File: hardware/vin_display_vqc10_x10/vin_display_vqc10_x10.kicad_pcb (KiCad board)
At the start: 4 copper layers, 148 x 52 mm, 109 parts, among them J1 DEBUG, J2 USB_B_Micro, J3 DEBUG_UART, J4 IF_UART, J5 AUX_CONNECTOR, J6 Conn_01x02, Q1 BSS138, Q2 DMP2022LSS, Q3 DMP2022LSS, Q4 DMP2022LSS, Q5 DMP2022LSS, Q6 DMP2022LSS, Q7 DMG2301L, SW1 SW_RESET, SW2 BOOTSEL, SW3 KNOB, U1 W25Q16JVSNIQ, U10 HDSP-2000, U11 HDSP-2000, U12 HDSP-2000, U13 HDSP-2000, U14 HDSP-2000, U15 HDSP-2000, U16 HDSP-2000, U17 HDSP-2000, U18 HDSP-2000, U19 HDSP-2000, U2 MIC23050-SYML, U20 HDSP-2000, U21 HDSP-2000, U22 HDSP-2000, U23 HDSP-2000, U24 HDSP-2000, U3 RP2040, U5 HDSP-2000, U6 HDSP-2000, U7 HDSP-2000, U8 HDSP-2000, U9 HDSP-2000, X1 12MHz

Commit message: routing vqc10_x10
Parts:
- removed C28, C29, C30, C31, C32, C38, C39, C40, C41, C42: 0.1u, Capacitor_SMD:C_0603_1608Metric
- removed JP1: SolderJumper_3_Open, components:Solder_jumber_3pad
- removed Q7: DMG2301L, Package_TO_SOT_SMD:SOT-23
- removed R13: 100K, Resistor_SMD:R_0603_1608Metric
- removed U17, U18, U19, U20, U21, U22, U23, U24: HDSP-2000, components:HDSP_DIP12
- added Q8: DMP2022LSS, components:SO8_MOSFET_S3G1D4, F.Cu at (144.5, 87.1)
- added Q9: DMP2022LSS, components:SO8_MOSFET_S3G1D4, F.Cu at (144.5, 81.1)
- added R21: 100K, Resistor_SMD:R_0603_1608Metric, F.Cu at (96.0, 97.4)
- added U4: VQC10, components:VQC10, B.Cu at (341.6, 94.7)
- R14: value 100R -> 10K; footprint Resistor_SMD:R_0603_1608Metric -> Capacitor_SMD:C_0603_1608Metric
- R15: value 100R -> 100K
- U10, U11, U12, U13, U5, U6, U7, U8, U9: value HDSP-2000 -> VQC10; footprint components:HDSP_DIP12 -> components:VQC10
- U14, U15, U16: value HDSP-2000 -> 74HCT154; footprint components:HDSP_DIP12 -> Package_SO:TSSOP-24_4.4x7.8mm_P0.65mm; moved to F.Cu
- moved U9 170.0 mm to (341.6, 122.4)
- moved C37 133.6 mm to (309.3, 124.5), turned to 0 degrees
- moved C27 132.6 mm to (309.3, 96.9), turned to 0 degrees
- moved SW1 97.9 mm to (320.2, 114.0)
- moved R1 97.7 mm to (334.5, 114.7)
- moved SW2 97.7 mm to (329.1, 114.0)
- moved J5 96.7 mm to (113.3, 77.0)
- moved C33 96.2 mm to (147.8, 124.5)
- moved C23 94.6 mm to (147.8, 96.9)
- moved U14 89.6 mm to (263.8, 86.3), turned to -90 degrees
- moved C36 76.7 mm to (268.9, 124.6), turned to 0 degrees
- moved C26 74.9 mm to (269.0, 96.9), turned to 0 degrees
- moved R14 74.1 mm to (92.0, 99.9)
- moved R15 71.9 mm to (92.0, 102.4)
- moved U10 59.5 mm to (301.2, 122.4)
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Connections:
- J5 pad 4: GP14 -> GND
- J5 pad 6: GP15 -> GP18
- Q2 pad 2: DISP_COL1 -> DISP_R1
- Q2 pad 3: DRV_COL1 -> DRV_R1
- Q3 pad 2: DISP_COL2 -> DISP_R2
- Q3 pad 3: DRV_COL2 -> DRV_R2
- Q4 pad 2: DISP_COL3 -> DISP_R3
- Q4 pad 3: DRV_COL3 -> DRV_R3
- Q5 pad 2: DISP_COL4 -> DISP_R4
- Q5 pad 3: DRV_COL4 -> DRV_R4
- Q6 pad 2: DISP_COL5 -> DISP_R5
- Q6 pad 3: DRV_COL5 -> DRV_R5
- R14 pad 1: Net-(U24-DOUT) -> GND
- R14 pad 2: GND -> Net-(U16-Y10)
- R15 pad 1: D10_DOUT -> 3V3
- R15 pad 2: GND -> DISP_R1
- R16 pad 2: DISP_COL1 -> DISP_R2
- R17 pad 2: DISP_COL2 -> DISP_R3
- R18 pad 2: DISP_COL3 -> DISP_R4
- R19 pad 2: DISP_COL4 -> DISP_R5
- R20 pad 2: DISP_COL5 -> DISP_R6
- U10 pad 1: DRV_COL1 -> DISP_D1
- U10 pad 10: DISP_CLK -> GND
- U10 pad 11: GND -> DISP_D4
- U10 pad 12: D5_DOUT -> DISP_C28
- U10 pad 2: DRV_COL2 -> DISP_C25
- U10 pad 3: DRV_COL3 -> GND
- U10 pad 4: DRV_COL4 -> DISP_D3
- U10 pad 5: DRV_COL5 -> DISP_C26
- U10 pad 6: unconnected-(U10-NC-Pad6) -> GND
- U10 pad 7: Net-(U10-DOUT) -> unconnected-(U10-IV-Pad7)
- U10 pad 8: DISP_VB -> DISP_D2
- U10 pad 9: DISP_VCC -> DISP_C27
- U11 pad 1: DRV_COL1 -> DISP_D1
- U11 pad 10: DISP_CLK -> GND
- U11 pad 11: GND -> DISP_D4
- U11 pad 12: Net-(U10-DOUT) -> DISP_C32
- U11 pad 2: DRV_COL2 -> DISP_C29
- U11 pad 3: DRV_COL3 -> GND
- U11 pad 4: DRV_COL4 -> DISP_D3
- U11 pad 5: DRV_COL5 -> DISP_C30
- U11 pad 6: unconnected-(U11-NC-Pad6) -> GND
- U11 pad 7: Net-(U11-DOUT) -> unconnected-(U11-IV-Pad7)
- U11 pad 8: DISP_VB -> DISP_D2
- U11 pad 9: DISP_VCC -> DISP_C31
- U12 pad 1: DRV_COL1 -> DISP_D1
- U12 pad 10: DISP_CLK -> GND
- U12 pad 11: GND -> DISP_D4
- U12 pad 12: Net-(U11-DOUT) -> DISP_C36
- U12 pad 2: DRV_COL2 -> DISP_C33
- U12 pad 3: DRV_COL3 -> GND
- U12 pad 4: DRV_COL4 -> DISP_D3
- U12 pad 5: DRV_COL5 -> DISP_C34
- U12 pad 6: unconnected-(U12-NC-Pad6) -> GND
- U12 pad 7: Net-(U12-DOUT) -> unconnected-(U12-IV-Pad7)
- U12 pad 8: DISP_VB -> DISP_D2
- U12 pad 9: DISP_VCC -> DISP_C35
- U13 pad 1: DRV_COL1 -> DISP_D1
- U13 pad 10: DISP_CLK -> GND
- U13 pad 11: GND -> DISP_D4
- U13 pad 12: Net-(U12-DOUT) -> DISP_C40
- U13 pad 2: DRV_COL2 -> DISP_C37
- U13 pad 3: DRV_COL3 -> GND
- U13 pad 4: DRV_COL4 -> DISP_D3
- U13 pad 5: DRV_COL5 -> DISP_C38
- U13 pad 6: unconnected-(U13-NC-Pad6) -> GND
- U13 pad 7: Net-(U13-DOUT) -> unconnected-(U13-IV-Pad7)
- U13 pad 8: DISP_VB -> DISP_D2
- U13 pad 9: DISP_VCC -> DISP_C39
- U14 pad 1: DRV_COL1 -> DISP_C1
- U14 pad 10: DISP_CLK -> DISP_C10
- U14 pad 11: GND -> DISP_C11
- U14 pad 12: Net-(U13-DOUT) -> GND
- U14 pad 2: DRV_COL2 -> DISP_C2
- U14 pad 3: DRV_COL3 -> DISP_C3
- U14 pad 4: DRV_COL4 -> DISP_C4
- U14 pad 5: DRV_COL5 -> DISP_C5
- U14 pad 6: unconnected-(U14-NC-Pad6) -> DISP_C6
- U14 pad 7: D10_DOUT -> DISP_C7
- U14 pad 8: DISP_VB -> DISP_C8
- U14 pad 9: DISP_VCC -> DISP_C9
- U15 pad 1: DRV_COL1 -> DISP_C17
- U15 pad 10: DISP_CLK -> DISP_C26
- U15 pad 11: GND -> DISP_C27
- U15 pad 12: Net-(JP1-C) -> GND
- U15 pad 2: DRV_COL2 -> DISP_C18
- U15 pad 3: DRV_COL3 -> DISP_C19
- U15 pad 4: DRV_COL4 -> DISP_C20
- U15 pad 5: DRV_COL5 -> DISP_C21
- U15 pad 6: unconnected-(U15-NC-Pad6) -> DISP_C22
- U15 pad 7: Net-(U15-DOUT) -> DISP_C23
- U15 pad 8: DISP_VB -> DISP_C24
- U15 pad 9: DISP_VCC -> DISP_C25
- U16 pad 1: DRV_COL1 -> DISP_C33
- U16 pad 10: DISP_CLK -> Net-(U16-Y10)
- U16 pad 11: GND -> Net-(U16-Y10)
- U16 pad 12: Net-(U15-DOUT) -> GND
- U16 pad 2: DRV_COL2 -> DISP_C34
- U16 pad 3: DRV_COL3 -> DISP_C35
- U16 pad 4: DRV_COL4 -> DISP_C36
- U16 pad 5: DRV_COL5 -> DISP_C37
- U16 pad 6: unconnected-(U16-NC-Pad6) -> DISP_C38
- U16 pad 7: Net-(U16-DOUT) -> DISP_C39
- U16 pad 8: DISP_VB -> DISP_C40
- U16 pad 9: DISP_VCC -> Net-(U16-Y10)
- U3 pad 11: DISP_COL2 -> DISP_R3
- U3 pad 12: DISP_COL3 -> DISP_R4
- U3 pad 13: DISP_COL4 -> DISP_R5
- U3 pad 14: DISP_COL5 -> DISP_R6
- U3 pad 15: DISP_BR -> DISP_R7
- U3 pad 16: GP13 -> DISP_C_E3
- U3 pad 17: GP14 -> DISP_C_A0
- U3 pad 18: GP15 -> DISP_C_A1
- U3 pad 27: GP16 -> DISP_C_A2
- U3 pad 28: GP17 -> DISP_C_A3
- U3 pad 30: GP19 -> DISP_D1
- U3 pad 31: GP20 -> DISP_D2
- U3 pad 32: GP21 -> DISP_D3
- U3 pad 34: GP22 -> DISP_D4
- U3 pad 35: GP23 -> DISP_D5
- U3 pad 4: DISP_DATA -> DISP_C_E1
- U3 pad 5: DISP_DATA2 -> DISP_C_E2
- U3 pad 8: DISP_CLK -> DISP_R1
- U3 pad 9: DISP_COL1 -> DISP_R2
- U5 pad 1: DRV_COL1 -> DISP_D1
- U5 pad 10: DISP_CLK -> GND
- U5 pad 11: GND -> DISP_D4
- U5 pad 12: DISP_DATA -> DISP_C8
- U5 pad 2: DRV_COL2 -> DISP_C5
- U5 pad 3: DRV_COL3 -> GND
- U5 pad 4: DRV_COL4 -> DISP_D3
- U5 pad 5: DRV_COL5 -> DISP_C6
- U5 pad 6: unconnected-(U5-NC-Pad6) -> GND
- U5 pad 7: Net-(U5-DOUT) -> unconnected-(U5-IV-Pad7)
- U5 pad 8: DISP_VB -> DISP_D2
- U5 pad 9: DISP_VCC -> DISP_C7
- U6 pad 1: DRV_COL1 -> DISP_D1
- U6 pad 10: DISP_CLK -> GND
- U6 pad 11: GND -> DISP_D4
- U6 pad 12: Net-(U5-DOUT) -> DISP_C12
- U6 pad 2: DRV_COL2 -> DISP_C9
- U6 pad 3: DRV_COL3 -> GND
- U6 pad 4: DRV_COL4 -> DISP_D3
- U6 pad 5: DRV_COL5 -> DISP_C10
- U6 pad 6: unconnected-(U6-NC-Pad6) -> GND
- U6 pad 7: Net-(U6-DOUT) -> unconnected-(U6-IV-Pad7)
- U6 pad 8: DISP_VB -> DISP_D2
- U6 pad 9: DISP_VCC -> DISP_C11
- U7 pad 1: DRV_COL1 -> DISP_D1
- U7 pad 10: DISP_CLK -> GND
- U7 pad 11: GND -> DISP_D4
- U7 pad 12: Net-(U6-DOUT) -> DISP_C16
- U7 pad 2: DRV_COL2 -> DISP_C13
- U7 pad 3: DRV_COL3 -> GND
- U7 pad 4: DRV_COL4 -> DISP_D3
- U7 pad 5: DRV_COL5 -> DISP_C14
- U7 pad 6: unconnected-(U7-NC-Pad6) -> GND
- U7 pad 7: Net-(U7-DOUT) -> unconnected-(U7-IV-Pad7)
- U7 pad 8: DISP_VB -> DISP_D2
- U7 pad 9: DISP_VCC -> DISP_C15
- U8 pad 1: DRV_COL1 -> DISP_D1
- U8 pad 10: DISP_CLK -> GND
- U8 pad 11: GND -> DISP_D4
- U8 pad 12: Net-(U7-DOUT) -> DISP_C20
- U8 pad 2: DRV_COL2 -> DISP_C17
- U8 pad 3: DRV_COL3 -> GND
- U8 pad 4: DRV_COL4 -> DISP_D3
- U8 pad 5: DRV_COL5 -> DISP_C18
- U8 pad 6: unconnected-(U8-NC-Pad6) -> GND
- U8 pad 7: Net-(U8-DOUT) -> unconnected-(U8-IV-Pad7)
- U8 pad 8: DISP_VB -> DISP_D2
- U8 pad 9: DISP_VCC -> DISP_C19
- U9 pad 1: DRV_COL1 -> DISP_D1
- U9 pad 10: DISP_CLK -> GND
- U9 pad 11: GND -> DISP_D4
- U9 pad 12: Net-(U8-DOUT) -> DISP_C24
- U9 pad 2: DRV_COL2 -> DISP_C21
- U9 pad 3: DRV_COL3 -> GND
- U9 pad 4: DRV_COL4 -> DISP_D3
- U9 pad 5: DRV_COL5 -> DISP_C22
- U9 pad 6: unconnected-(U9-NC-Pad6) -> GND
- U9 pad 7: D5_DOUT -> unconnected-(U9-IV-Pad7)
- U9 pad 8: DISP_VB -> DISP_D2
- U9 pad 9: DISP_VCC -> DISP_C23
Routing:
- net DRV_COL1: track 469.9 -> 0.00 mm, vias 21 -> 0
- net DRV_R5: track 0.00 -> 468.4 mm, vias 0 -> 10
- net DRV_COL2: track 450.5 -> 0.00 mm, vias 24 -> 0
- net DRV_R4: track 0.00 -> 427.2 mm, vias 0 -> 10
- net DRV_R2: track 0.00 -> 422.1 mm, vias 0 -> 12
- net DRV_COL3: track 420.1 -> 0.00 mm, vias 16 -> 0
- net DRV_R1: track 0.00 -> 394.6 mm, vias 0 -> 8
- net DRV_COL4: track 392.7 -> 0.00 mm, vias 23 -> 0
- net DISP_CLK: track 389.1 -> 0.00 mm, vias 1 -> 0
- net DRV_R3: track 0.00 -> 385.8 mm, vias 0 -> 8
- net DRV_R6: track 0.00 -> 373.5 mm, vias 0 -> 10
- net DRV_COL5: track 372.0 -> 0.00 mm, vias 6 -> 0
- net DRV_R7: track 0.00 -> 367.3 mm, vias 0 -> 2
- net DISP_D1: track 0.00 -> 357.2 mm, vias 0 -> 8
- net DISP_D3: track 0.00 -> 351.5 mm, vias 0 -> 8
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- removed copper zone on F.Cu, net DISP_VCC
- removed copper zone on F.Cu, net VSYS
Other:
- board size 148 x 52 mm -> 241.5 x 55.3 mm

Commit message: route vqc10_x10 board
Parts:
- moved D1 73.4 mm to (51.4, 101.5)
- moved J1 73.2 mm to (40.7, 104.2)
- moved SW1 73.1 mm to (249.9, 94.2)
- moved C1 73.0 mm to (45.3, 87.4)
- moved C10 73.0 mm to (70.2, 88.3)
- moved C12 73.0 mm to (62.4, 97.2)
- moved C14 73.0 mm to (45.3, 89.0)
- moved C15 73.0 mm to (36.6, 81.2)
- moved C16 73.0 mm to (35.8, 87.3)
- moved C17 73.0 mm to (38.6, 84.0)
- moved C2 73.0 mm to (56.1, 96.0)
- moved C20 73.0 mm to (49.3, 80.0)
- moved C21 73.0 mm to (68.8, 79.4)
- moved C22 73.0 mm to (63.0, 79.4)
- moved C25 73.0 mm to (158.3, 77.2)
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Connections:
- U14 pad 24: Net-(U14-VCC) -> DISP_VCC
- U15 pad 24: Net-(U14-VCC) -> DISP_VCC
- U16 pad 24: Net-(U14-VCC) -> DISP_VCC
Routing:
- net Net-(U1-CS): track 31.1 -> 231.0 mm, vias 2 -> 5
- net Net-(U3-RUN): track 24.1 -> 208.8 mm, vias 1 -> 5
- net DISP_C_A3: track 100.4 -> 242.3 mm, vias 0 -> 8
- net DISP_C_A2: track 101.1 -> 242.6 mm, vias 0 -> 9
- net DISP_C_E2: track 8.27 -> 145.7 mm, vias 2 -> 5
- net DISP_C20: track 0.00 -> 132.5 mm, vias 0 -> 1
- net DISP_C19: track 0.00 -> 123.6 mm, vias 0 -> 1
- net DISP_C_A1: track 112.6 -> 230.0 mm, vias 1 -> 8
- net DISP_C18: track 0.00 -> 114.1 mm, vias 0 -> 1
- net DISP_C_A0: track 109.0 -> 216.3 mm, vias 3 -> 10
- net DISP_D2: track 344.1 -> 451.2 mm, vias 8 -> 12
- net VSYS: track 27.0 -> 132.2 mm
- net DISP_C17: track 0.00 -> 104.3 mm, vias 0 -> 1
- net UART1_RX: track 18.0 -> 117.8 mm
- net DISP_D3: track 351.5 -> 450.4 mm, vias 8 -> 10
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- added copper zone on F.Cu, net DISP_VCC
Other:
- board size 241.5 x 55.3 mm -> 242 x 55 mm
- board text added: "DIO/GND/CLK"
- board text added: "R15-R21"
- board text removed: "DIO/GNF/CLK"

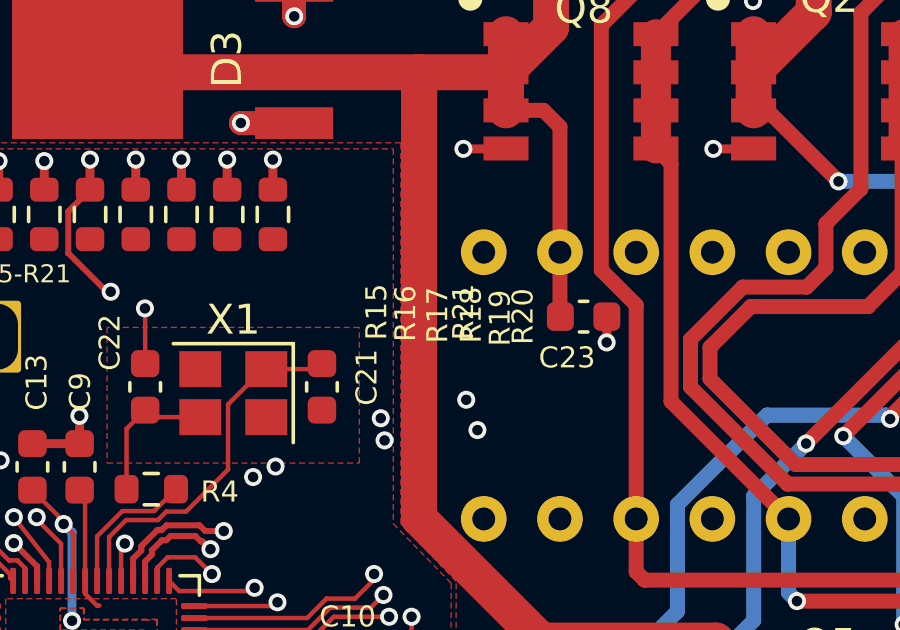
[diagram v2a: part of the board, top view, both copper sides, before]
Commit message: minor fixes in vqc10_x10 and hdsp2000_x20 pcb/schematics
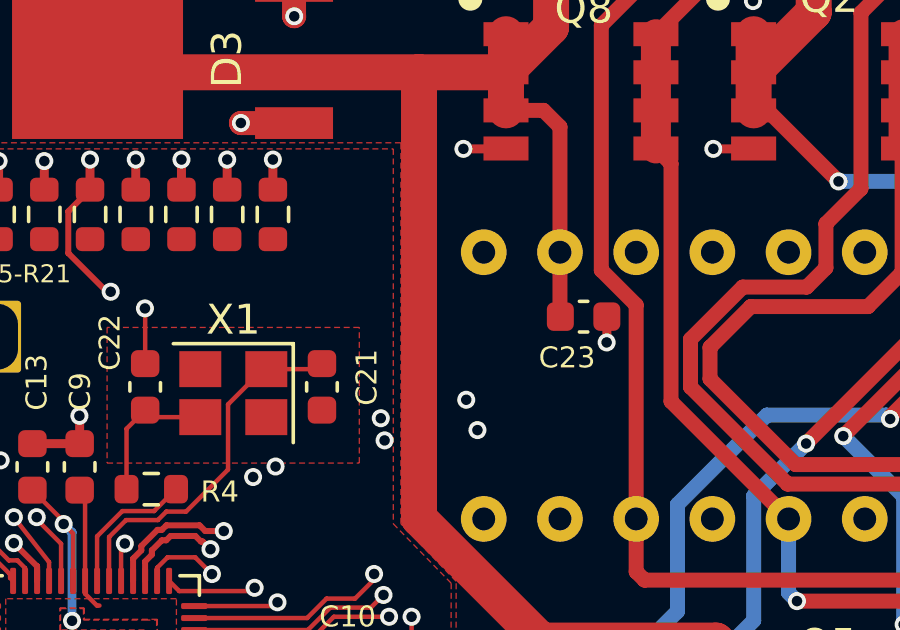
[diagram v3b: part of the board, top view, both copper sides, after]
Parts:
- Q2, Q3, Q4, Q5, Q6, Q8, Q9: value DMP2022LSS -> SQ4435EY
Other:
- board text added: "VinDisplay vqc10_x10 v1.0"
- board text removed: "VinDisplay hdsp2000_x20 v1.0"
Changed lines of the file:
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@@
     (property "ki_keywords" "R res resistor")
     (attr smd)
-    (fp_text reference "R17" (at -3.3528 13.1064 90) (layer "F.SilkS")
+    (fp_text reference "R17" (at -3.3528 13.1064 90) (layer "F.SilkS") hide
         (effects (font (size 0.7 0.7) (thickness 0.15)))
     )
@@
         (effects (font (size 1 1) (thickness 0.1)))
     )
-    (fp_text value "DMP2022LSS" (at 2.54 2.54 -90 unlocked) (layer "F.Fab")
+    (fp_text value "SQ4435EY" (at 2.54 2.54 -90 unlocked) (layer "F.Fab")
         (effects (font (size 1 1) (thickness 0.15)))
     )
@@
         (effects (font (size 1 1) (thickness 0.1)))
     )
-    (fp_text value "DMP2022LSS" (at 2.54 2.54 -90 unlocked) (layer "F.Fab")
+    (fp_text value "SQ4435EY" (at 2.54 2.54 -90 unlocked) (layer "F.Fab")
         (effects (font (size 1 1) (thickness 0.15)))
     )
@@
         (effects (font (size 1 1) (thickness 0.1)))
     )
-    (fp_text value "DMP2022LSS" (at 2.54 2.54 -90 unlocked) (layer "F.Fab")
+    (fp_text value "SQ4435EY" (at 2.54 2.54 -90 unlocked) (layer "F.Fab")
         (effects (font (size 1 1) (thickness 0.15)))
     )
@@
     (property "ki_keywords" "R res resistor")
     (attr smd)
-    (fp_text reference "R19" (at -3.4544 7.5692 90) (layer "F.SilkS")
+    (fp_text reference "R19" (at -3.4544 7.5692 90) (layer "F.SilkS") hide
         (effects (font (size 0.7 0.7) (thickness 0.15)))
     )
@@
         (effects (font (size 1 1) (thickness 0.1)))
     )
-    (fp_text value "DMP2022LSS" (at 2.54 2.54 -90 unlocked) (layer "F.Fab")
+    (fp_text value "SQ4435EY" (at 2.54 2.54 -90 unlocked) (layer "F.Fab")
         (effects (font (size 1 1) (thickness 0.15)))
     )
@@
         (effects (font (size 1 1) (thickness 0.1)))
     )
-    (fp_text value "DMP2022LSS" (at 2.54 2.54 -90 unlocked) (layer "F.Fab")
+    (fp_text value "SQ4435EY" (at 2.54 2.54 -90 unlocked) (layer "F.Fab")
         (effects (font (size 1 1) (thickness 0.15)))
     )
@@
     (property "ki_keywords" "R res resistor")
     (attr smd)
-    (fp_text reference "R18" (at -3.3528 8.128 90) (layer "F.SilkS")
+    (fp_text reference "R18" (at -3.3528 8.128 90) (layer "F.SilkS") hide
         (effects (font (size 0.7 0.7) (thickness 0.15)))
     )
@@
     (property "ki_keywords" "R res resistor")
     (attr smd)
-    (fp_text reference "R16" (at -3.302 7.4676 90) (layer "F.SilkS")
+    (fp_text reference "R16" (at -3.302 7.4676 90) (layer "F.SilkS") hide
         (effects (font (size 0.7 0.7) (thickness 0.15)))
     )
@@
     (property "ki_keywords" "R res resistor")
     (attr smd)
-    (fp_text reference "R20" (at -3.4036 14.4272 90) (layer "F.SilkS")
+    (fp_text reference "R20" (at -3.4036 14.4272 90) (layer "F.SilkS") hide
         (effects (font (size 0.7 0.7) (thickness 0.15)))
     )
@@
         (effects (font (size 1 1) (thickness 0.1)))
     )
-    (fp_text value "DMP2022LSS" (at 2.54 2.54 -90 unlocked) (layer "F.Fab")
+    (fp_text value "SQ4435EY" (at 2.54 2.54 -90 unlocked) (layer "F.Fab")
         (effects (font (size 1 1) (thickness 0.15)))
     )
@@
     (property "ki_keywords" "R res resistor")
     (attr smd)
-    (fp_text reference "R15" (at -3.2512 8.0264 90) (layer "F.SilkS")
+    (fp_text reference "R15" (at -3.2512 8.0264 90) (layer "F.SilkS") hide
         (effects (font (size 0.7 0.7) (thickness 0.15)))
     )
@@
         (effects (font (size 1 1) (thickness 0.1)))
     )
-    (fp_text value "DMP2022LSS" (at 2.54 2.54 -90 unlocked) (layer "F.Fab")
+    (fp_text value "SQ4435EY" (at 2.54 2.54 -90 unlocked) (layer "F.Fab")
         (effects (font (size 1 1) (thickness 0.15)))
     )
@@
     (property "ki_keywords" "R res resistor")
     (attr smd)
-    (fp_text reference "R21" (at -3.2512 15.494 90) (layer "F.SilkS")
+    (fp_text reference "R21" (at -3.2512 15.494 90) (layer "F.SilkS") hide
         (effects (font (size 0.7 0.7) (thickness 0.15)))
     )
@@
     (effects (font (size 1.5 1.5) (thickness 0.3) bold) (justify left bottom mirror))
   )
-  (gr_text "VinDisplay hdsp2000_x20 v1.0" (at 270.2288 69.3424) (layer "B.SilkS")
+  (gr_text "VinDisplay vqc10_x10 v1.0" (at 270.2288 69.3424) (layer "B.SilkS")
     (effects (font (size 1.5 1.5) (thickness 0.3) bold) (justify left bottom mirror))
   )
